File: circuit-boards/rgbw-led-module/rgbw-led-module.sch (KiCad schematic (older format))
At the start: 5 parts

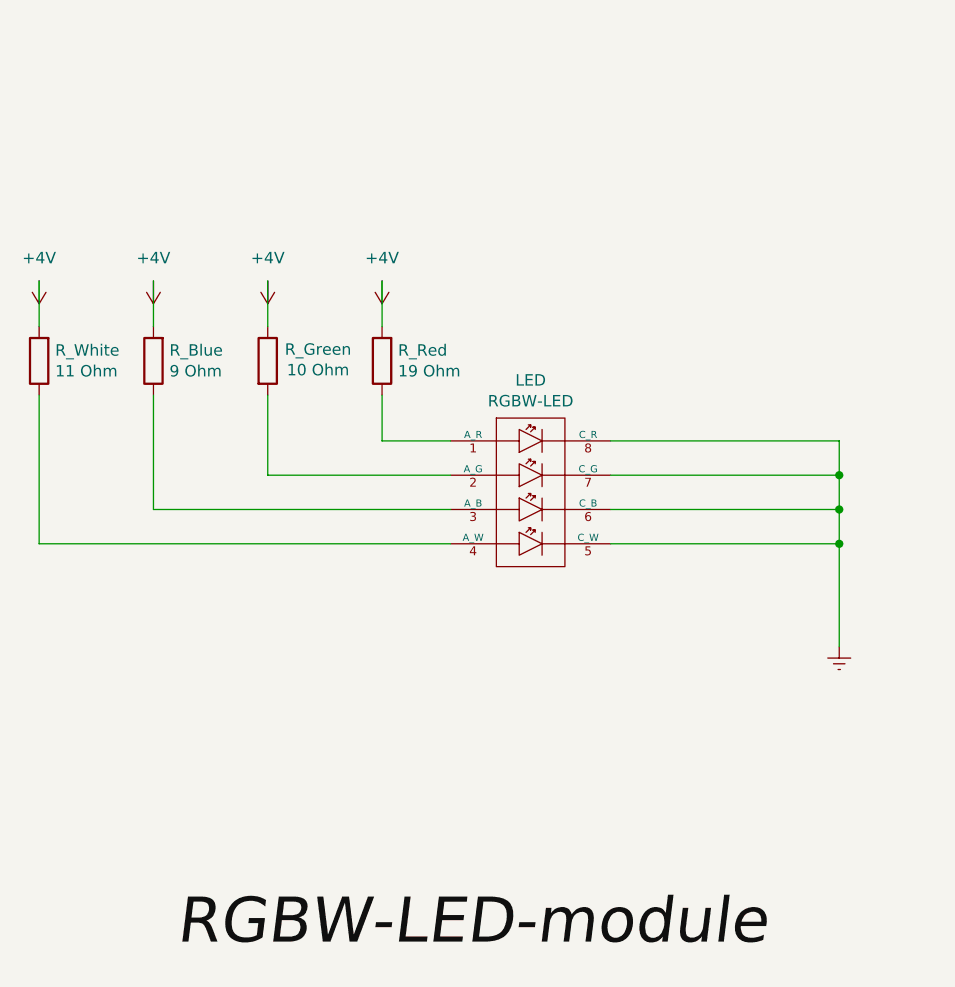
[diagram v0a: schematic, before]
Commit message: Updated version of the board which actually goes through DRC checks.
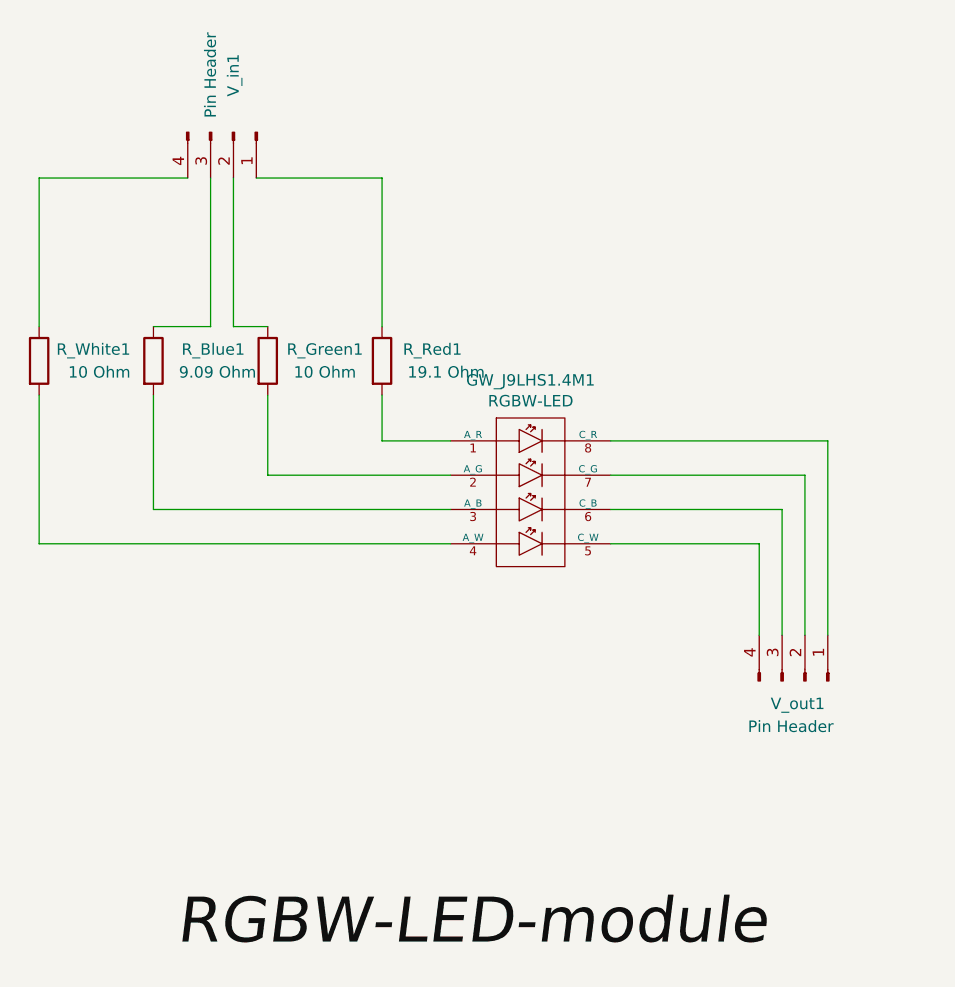
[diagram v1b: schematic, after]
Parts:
- removed LED: RGBW-LED, symbol bioreactor:RGBW-LED
- added GW_J9LHS1.4M1: RGBW-LED, bioreactor:RGBW_LED_GW_J9LHS1.4M_HandSolder, symbol bioreactor:RGBW-LED
- added V_in1, V_out1: Pin Header, Connector_PinHeader_2.54mm:PinHeader_1x04_P2.54mm_Vertical, symbol Connector:Conn_01x04_Male
- R_Blue1: renamed from R_Blue; value 9 Ohm -> 9.09 Ohm; footprint (none) -> Resistor_SMD:R_1206_3216Metric_Pad1.30x1.75mm_HandSolder
- R_Green1: renamed from R_Green; footprint (none) -> Resistor_SMD:R_1206_3216Metric_Pad1.30x1.75mm_HandSolder
- R_Red1: renamed from R_Red; value 19 Ohm -> 19.1 Ohm; footprint (none) -> Resistor_SMD:R_1206_3216Metric_Pad1.30x1.75mm_HandSolder
- R_White1: renamed from R_White; value 11 Ohm -> 10 Ohm; footprint (none) -> Resistor_SMD:R_1206_3216Metric_Pad1.30x1.75mm_HandSolder
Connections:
- net at R_Red1.1: now also V_in1.1 (Pin_1)
- net at R_Green1.2: now also GW_J9LHS1.4M1.2 (A_G)
- net at R_Blue1.1: now also V_in1.3 (Pin_3)
- net at R_White1.1: now also V_in1.4 (Pin_4)
- removed net +4V: R_Blue1.2, R_Green1.1, R_Red1.2, R_White1.2
- new net: GW_J9LHS1.4M1.1 (A_R), R_Red1.2
- new net: R_Green1.1, V_in1.2 (Pin_2)
- new net: GW_J9LHS1.4M1.4 (A_W), R_White1.2
- new net: GW_J9LHS1.4M1.3 (A_B), R_Blue1.2
- new net: GW_J9LHS1.4M1.5 (C_W), V_out1.4 (Pin_4)
- new net: GW_J9LHS1.4M1.6 (C_B), V_out1.3 (Pin_3)
- new net: GW_J9LHS1.4M1.7 (C_G), V_out1.2 (Pin_2)
- new net: GW_J9LHS1.4M1.8 (C_R), V_out1.1 (Pin_1)
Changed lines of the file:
@@
 RGBW-LED-module
 $Comp
-L bioreactor:RGBW-LED LED
-U 1 1 619B862E
-P 3350 2600
-F 0 "LED" H 3350 3115 50  0000 C CNN
-F 1 "RGBW-LED" H 3350 3024 50  0000 C CNN
-F 2 "" H 3350 2600 50  0001 C CNN
-F 3 "" H 3350 2600 50  0001 C CNN
-	1    3350 2600
+L Device:R R_Red1
+U 1 1 619BC99C
+P 2700 2000
+F 0 "R_Red1" H 3050 2050 50  0000 R CNN
+F 1 "19.1 Ohm" H 3150 1950 50  0000 R CNN
+F 2 "Resistor_SMD:R_1206_3216Metric_Pad1.30x1.75mm_HandSolder" V 2630 2000 50  0001 C CNN
+F 3 "https://cz.mouser.com/datasheet/2/427/dcrcwe3-1762152.pdf" H 2700 2000 50  0001 C CNN
+	1    2700 2000
 	1    0    0    -1
 $EndComp
 $Comp
-L Device:R R_Red
-U 1 1 619BC99C
-P 2700 2000
-F 0 "R_Red" H 2630 1954 50  0000 R CNN
-F 1 "19 Ohm" H 2630 2045 50  0000 R CNN
-F 2 "" V 2630 2000 50  0001 C CNN
-F 3 "~" H 2700 2000 50  0001 C CNN
-	1    2700 2000
-	-1   0    0    1
+L Device:R R_White1
+U 1 1 619BD14C
+P 1200 2000
+F 0 "R_White1" H 1600 2050 50  0000 R CNN
+F 1 "10 Ohm" H 1600 1950 50  0000 R CNN
+F 2 "Resistor_SMD:R_1206_3216Metric_Pad1.30x1.75mm_HandSolder" V 1130 2000 50  0001 C CNN
+F 3 "https://cz.mouser.com/datasheet/2/427/crcwce3-1762584.pdf" H 1200 2000 50  0001 C CNN
+	1    1200 2000
+	1    0    0    -1
 $EndComp
 $Comp
-L Device:R R_White
-U 1 1 619BD14C
-P 1200 2000
-F 0 "R_White" H 1130 1954 50  0000 R CNN
-F 1 "11 Ohm" H 1130 2045 50  0000 R CNN
-F 2 "" V 1130 2000 50  0001 C CNN
-F 3 "~" H 1200 2000 50  0001 C CNN
-	1    1200 2000
-	-1   0    0    1
+L Device:R R_Blue1
+U 1 1 619BD683
+P 1700 2000
+F 0 "R_Blue1" H 2100 2050 50  0000 R CNN
+F 1 "9.09 Ohm" H 2150 1950 50  0000 R CNN
+F 2 "Resistor_SMD:R_1206_3216Metric_Pad1.30x1.75mm_HandSolder" V 1630 2000 50  0001 C CNN
+F 3 "https://cz.mouser.com/datasheet/2/427/dcrcwe3-1762152.pdf" H 1700 2000 50  0001 C CNN
+	1    1700 2000
+	1    0    0    -1
 $EndComp
 $Comp
-L Device:R R_Blue
-U 1 1 619BD683
-P 1700 2000
-F 0 "R_Blue" H 1630 1954 50  0000 R CNN
-F 1 "9 Ohm" H 1630 2045 50  0000 R CNN
-F 2 "" V 1630 2000 50  0001 C CNN
-F 3 "~" H 1700 2000 50  0001 C CNN
-	1    1700 2000
-	-1   0    0    1
-$EndComp
-$Comp
-L Device:R R_Green
+L Device:R R_Green1
 U 1 1 619BCD1C
 P 2200 2000
-F 0 "R_Green" H 2420 2050 50  0000 C CNN
-F 1 "10 Ohm" H 2420 1960 50  0000 C CNN
-F 2 "" V 2130 2000 50  0001 C CNN
-F 3 "~" H 2200 2000 50  0001 C CNN
+F 0 "R_Green1" H 2450 2050 50  0000 C CNN
+F 1 "10 Ohm" H 2450 1950 50  0000 C CNN
+F 2 "Resistor_SMD:R_1206_3216Metric_Pad1.30x1.75mm_HandSolder" V 2130 2000 50  0001 C CNN
+F 3 "https://cz.mouser.com/datasheet/2/427/crcwce3-1762584.pdf" H 2200 2000 50  0001 C CNN
 	1    2200 2000
 	1    0    0    -1
@@
 	1200 2800 3000 2800
 $Comp
-L power:+4V #PWR?
-U 1 1 619D96E5
-P 1200 1650
-F 0 "#PWR?" H 1200 1500 50  0001 C CNN
-F 1 "+4V" H 1200 1550 50  0000 C CNN
-F 2 "" H 1200 1650 50  0001 C CNN
-F 3 "" H 1200 1650 50  0001 C CNN
-	1    1200 1650
-	-1   0    0    1
+L bioreactor:RGBW-LED GW_J9LHS1.4M1
+U 1 1 61A86FD6
+P 3350 2600
+F 0 "GW_J9LHS1.4M1" H 3350 3115 50  0000 C CNN
+F 1 "RGBW-LED" H 3350 3024 50  0000 C CNN
+F 2 "bioreactor:RGBW_LED_GW_J9LHS1.4M_HandSolder" H 3350 2600 50  0001 C CNN
+F 3 "https://media.osram.info/media/resource/hires/osram-dam-15524600/GW+J9LHS1.4M_EN.pdf" H 3350 2600 50  0001 C CNN
+	1    3350 2600
+	1    0    0    -1
+$EndComp
+$Comp
+L Connector:Conn_01x04_Male V_in1
+U 1 1 61A8C71B
+P 2050 1000
+F 0 "V_in1" H 1800 1000 50  0000 C CNN
+F 1 "Pin Header" H 1800 900 50  0000 C CNN
+F 2 "Connector_PinHeader_2.54mm:PinHeader_1x04_P2.54mm_Vertical" H 2050 1000 50  0001 C CNN
+F 3 "~" H 2050 1000 50  0001 C CNN
+	1    2050 1000
+	0    1    1    0
+$EndComp
+$Comp
+L Connector:Conn_01x04_Male V_out1
+U 1 1 61A8F3A8
+P 4550 3400
+F 0 "V_out1" V 4450 3250 50  0000 L CNN
+F 1 "Pin Header" V 4350 3150 50  0000 L CNN
+F 2 "Connector_PinHeader_2.54mm:PinHeader_1x04_P2.54mm_Vertical" H 4550 3400 50  0001 C CNN
+F 3 "~" H 4550 3400 50  0001 C CNN
+	1    4550 3400
+	0    1    -1   0
 $EndComp
 Wire Wire Line
-	1200 1850 1200 1650
-$Comp
-L power:+4V #PWR?
-U 1 1 619E066E
-P 1700 1650
-F 0 "#PWR?" H 1700 1500 50  0001 C CNN
-F 1 "+4V" H 1700 1550 50  0000 C CNN
-F 2 "" H 1700 1650 50  0001 C CNN
-F 3 "" H 1700 1650 50  0001 C CNN
-	1    1700 1650
-	-1   0    0    1
-$EndComp
-$Comp
-L power:+4V #PWR?
-U 1 1 619E0DD0
-P 2200 1650
-F 0 "#PWR?" H 2200 1500 50  0001 C CNN
-F 1 "+4V" H 2200 1550 50  0000 C CNN
-F 2 "" H 2200 1650 50  0001 C CNN
-F 3 "" H 2200 1650 50  0001 C CNN
-	1    2200 1650
-	-1   0    0    1
-$EndComp
-$Comp
-L power:+4V #PWR?
-U 1 1 619E1764
-P 2700 1650
-F 0 "#PWR?" H 2700 1500 50  0001 C CNN
-F 1 "+4V" H 2700 1550 50  0000 C CNN
-F 2 "" H 2700 1650 50  0001 C CNN
-F 3 "" H 2700 1650 50  0001 C CNN
-	1    2700 1650
-	-1   0    0    1
-$EndComp
+	3700 2350 4650 2350
 Wire Wire Line
-	1700 1650 1700 1850
+	4650 2350 4650 3200
 Wire Wire Line
-	2200 1650 2200 1850
+	3700 2500 4550 2500
 Wire Wire Line
-	2700 1650 2700 1850
-$Comp
-L power:Earth #PWR?
-U 1 1 619E4257
-P 4700 3250
-F 0 "#PWR?" H 4700 3000 50  0001 C CNN
-F 1 "Earth" H 4700 3100 50  0001 C CNN
-F 2 "" H 4700 3250 50  0001 C CNN
-F 3 "~" H 4700 3250 50  0001 C CNN
-	1    4700 3250
-	1    0    0    -1
-$EndComp
+	4550 2500 4550 3200
 Wire Wire Line
-	3700 2350 4700 2350
+	3700 2650 4450 2650
 Wire Wire Line
-	4700 2350 4700 2500
+	4450 2650 4450 3200
 Wire Wire Line
-	3700 2500 4700 2500
-Connection ~ 4700 2500
+	3700 2800 4350 2800
 Wire Wire Line
-	4700 2500 4700 2650
+	4350 2800 4350 3200
 Wire Wire Line
-	3700 2650 4700 2650
-Connection ~ 4700 2650
+	2150 1200 2700 1200
 Wire Wire Line
-	4700 2650 4700 2800
+	2050 1850 2200 1850
 Wire Wire Line
-	3700 2800 4700 2800
-Connection ~ 4700 2800
+	1950 1850 1700 1850
 Wire Wire Line
-	4700 2800 4700 3250
+	2700 1200 2700 1850
+Wire Wire Line
+	2050 1200 2050 1850
+Wire Wire Line
+	1950 1200 1950 1850
+Wire Wire Line
+	1200 1850 1200 1200
+Wire Wire Line
+	1200 1200 1850 1200
 $EndSCHEMATC
